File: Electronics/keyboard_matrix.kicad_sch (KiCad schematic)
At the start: 5 parts, among them SW1 SW_SPST, SW2 SW_SPST, U1 STM32C011F6Px

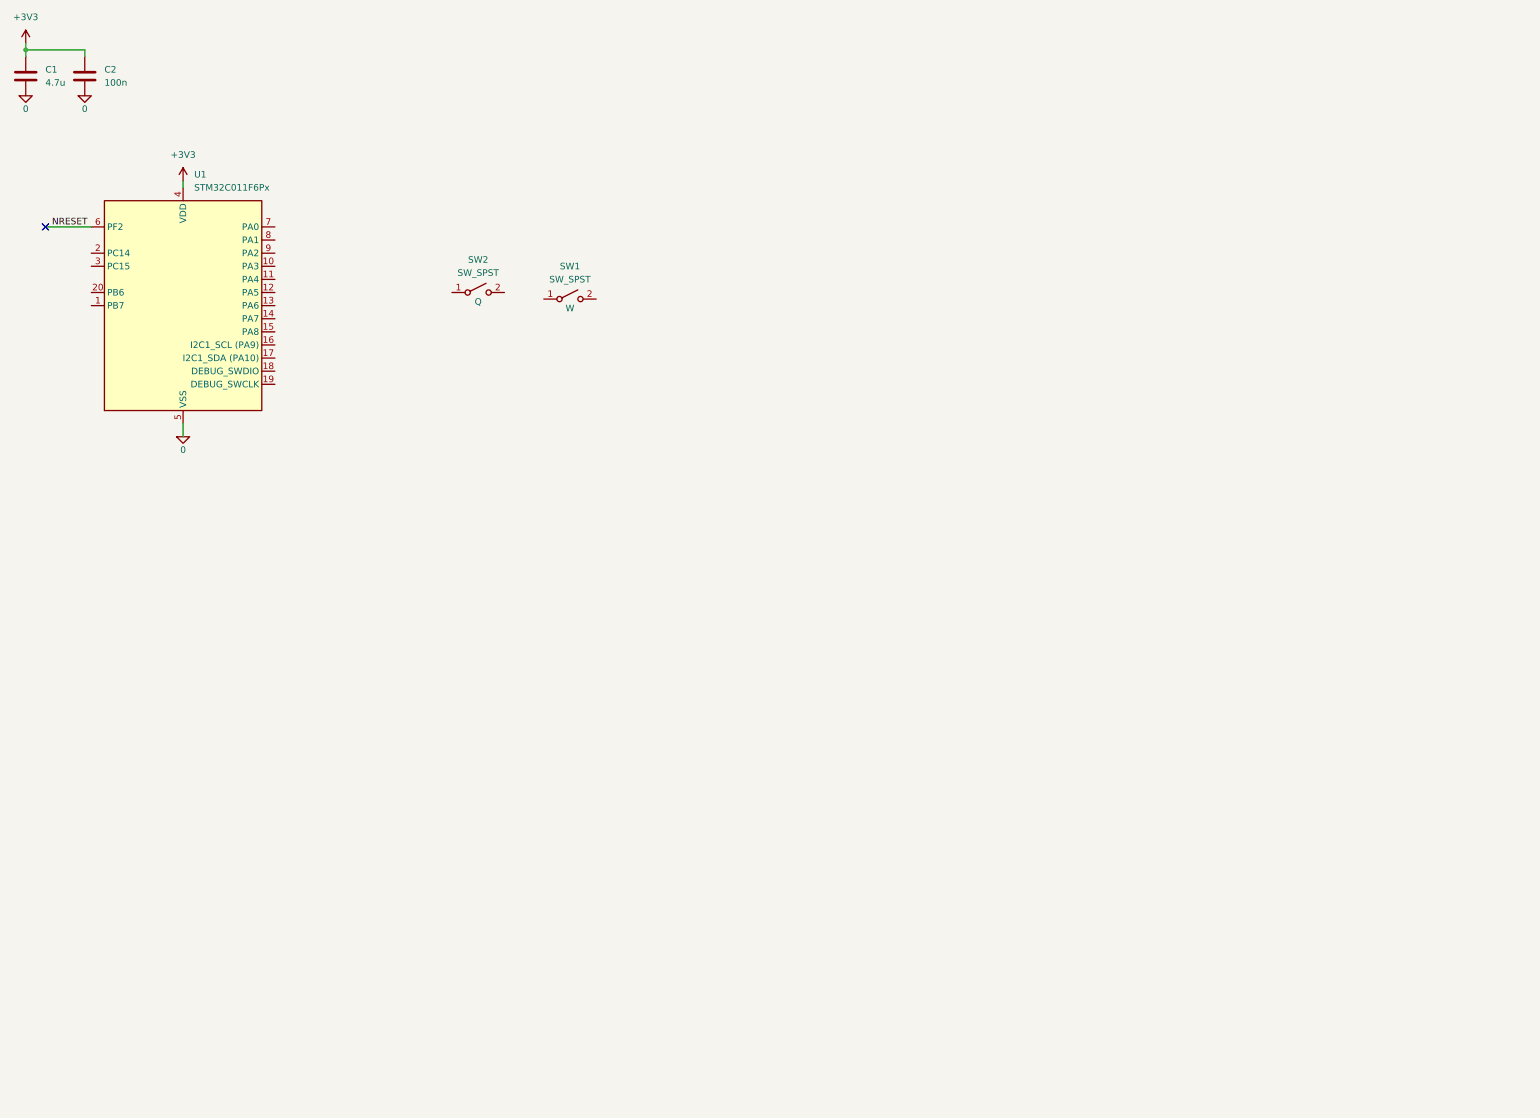
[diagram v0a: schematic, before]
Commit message: completed keyboard schematic. added design note for stm32c0
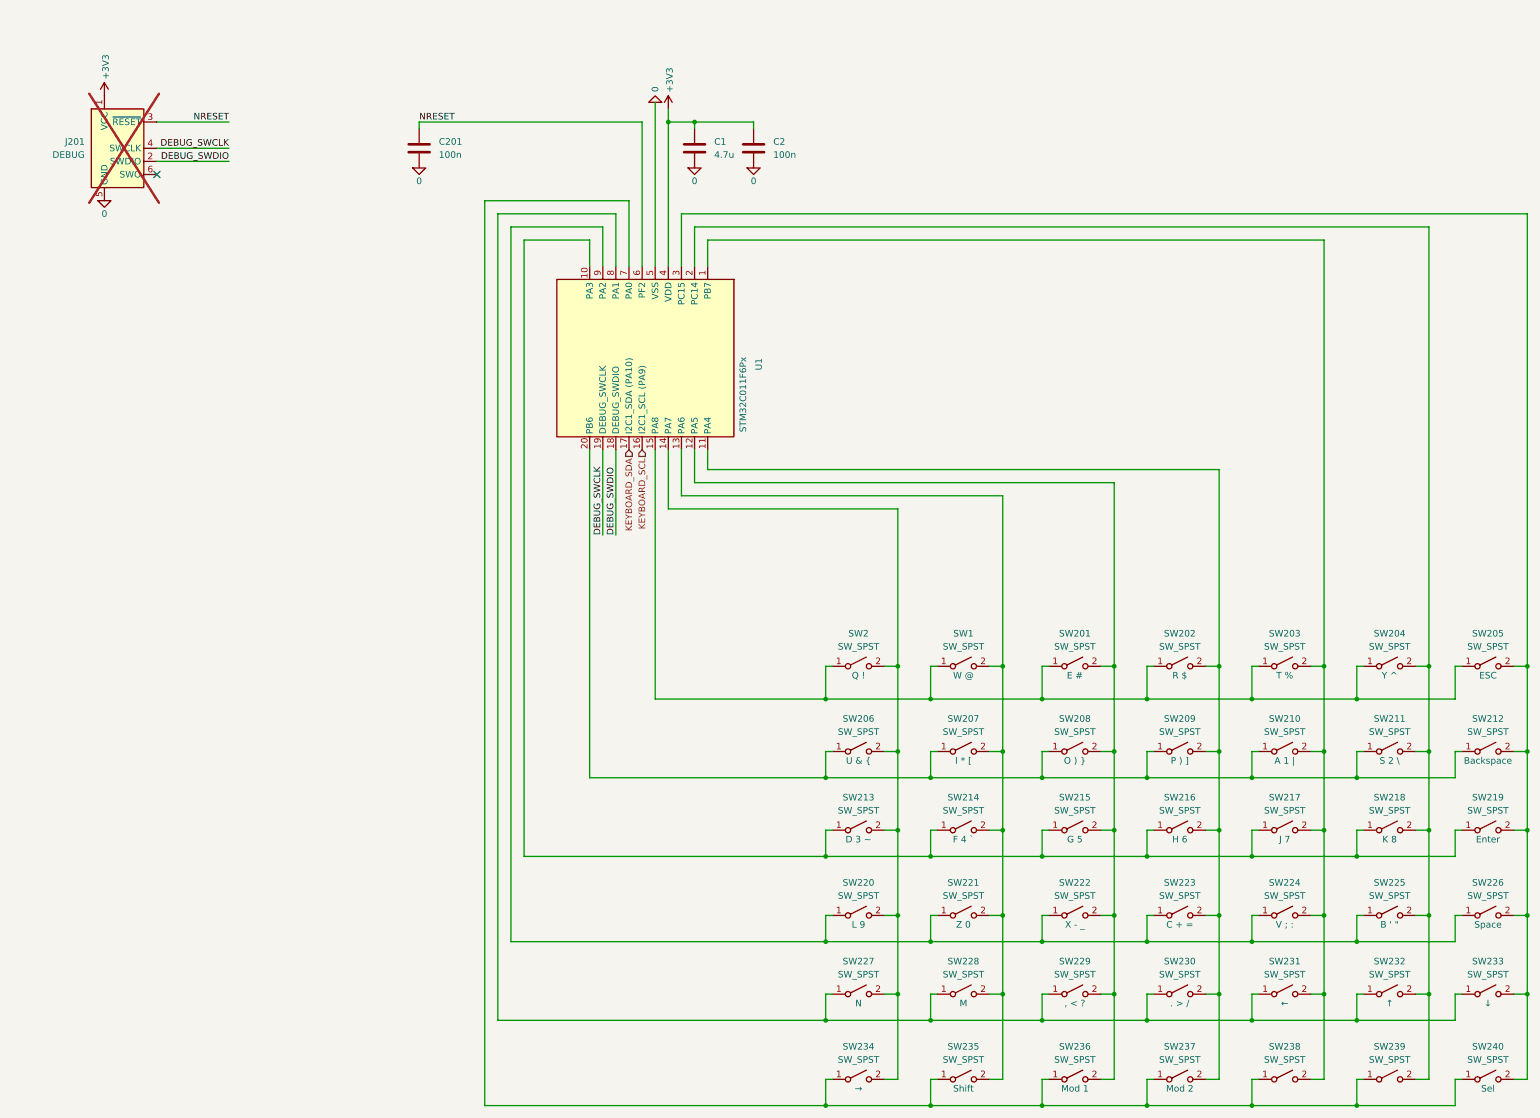
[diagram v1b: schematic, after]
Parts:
- added C201: 100n, Capacitor_SMD:C_0402_1005Metric_Pad0.74x0.62mm_HandSolder, symbol Device:C
- added J201: DEBUG, Connector:Tag-Connect_TC2030-IDC-FP_2x03_P1.27mm_Vertical, symbol Connector:Conn_ARM_SWD_TagConnect_TC2030
- added SW201, SW202, SW203, SW204, SW205, SW206, SW207, SW208, SW209, SW210, SW211, SW212, SW213, SW214, SW215, SW216, SW217, SW218, SW219, SW220, SW221, SW222, SW223, SW224, SW225, SW226, SW227, SW228, SW229, SW230, SW231, SW232, SW233, SW234, SW235, SW236, SW237, SW238, SW239, SW240: SW_SPST, Button_Switch_SMD:SW_Tactile_SPST_NO_Straight_CK_PTS636Sx25SMTRLFS, symbol Switch:SW_SPST
- SW1: Key Text W -> W @
- SW2: Key Text Q -> Q !
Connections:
- net +3V3: now also J201.1 (VCC)
- net 0: now also C201.2, J201.5 (GND)
- net NRESET: now also C201.1, J201.3 (~{RESET})
- net at SW2.1 (A): now also SW1.1 (A), U1.15 (PA8), SW201.1 (A), SW202.1 (A), SW203.1 (A), SW204.1 (A), SW205.1 (A)
- net at SW2.2 (B): now also U1.14 (PA7), SW206.2 (B), SW213.2 (B), SW220.2 (B), SW227.2 (B), SW234.2 (B)
- net at SW1.2 (B): now also U1.13 (PA6), SW207.2 (B), SW214.2 (B), SW221.2 (B), SW228.2 (B), SW235.2 (B)
- net at U1.1 (PB7): now also SW203.2 (B), SW210.2 (B), SW217.2 (B), SW224.2 (B), SW231.2 (B), SW238.2 (B)
- net at U1.10 (PA3): now also SW213.1 (A), SW214.1 (A), SW215.1 (A), SW216.1 (A), SW217.1 (A), SW218.1 (A), SW219.1 (A)
- net at U1.11 (PA4): now also SW202.2 (B), SW209.2 (B), SW216.2 (B), SW223.2 (B), SW230.2 (B), SW237.2 (B)
- net at U1.12 (PA5): now also SW201.2 (B), SW208.2 (B), SW215.2 (B), SW222.2 (B), SW229.2 (B), SW236.2 (B)
- net KEYBOARD_SCL: now reaches U1.16 (PA9/PA11)
- net KEYBOARD_SDA: now reaches U1.17 (PA10/PA12)
- net DEBUG_SWDIO: now reaches U1.18 (PA13)
- net DEBUG_SWDIO: now also J201.2 (SWDIO)
- net DEBUG_SWCLK: now reaches U1.19 (PA14)
- net DEBUG_SWCLK: now also J201.4 (SWCLK)
- net at U1.2 (PC14): now also SW204.2 (B), SW211.2 (B), SW218.2 (B), SW225.2 (B), SW232.2 (B), SW239.2 (B)
- net at U1.20 (PB6): now also SW206.1 (A), SW207.1 (A), SW208.1 (A), SW209.1 (A), SW210.1 (A), SW211.1 (A), SW212.1 (A)
- net at U1.3 (PC15): now also SW205.2 (B), SW212.2 (B), SW219.2 (B), SW226.2 (B), SW233.2 (B), SW240.2 (B)
- net at U1.7 (PA0): now also SW234.1 (A), SW235.1 (A), SW236.1 (A), SW237.1 (A), SW238.1 (A), SW239.1 (A), SW240.1 (A)
- net at U1.8 (PA1): now also SW227.1 (A), SW228.1 (A), SW229.1 (A), SW230.1 (A), SW231.1 (A), SW232.1 (A), SW233.1 (A)
- net at U1.9 (PA2): now also SW220.1 (A), SW221.1 (A), SW222.1 (A), SW223.1 (A), SW224.1 (A), SW225.1 (A), SW226.1 (A)
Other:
- company: (none) -> Bjorn Hropot
- title: (none) -> Keyboard
- moved on the sheet: C1, C2, SW1, SW2, U1

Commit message: arranged keys for keyboard. marked out lcd
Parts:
- SW40: renamed from SW238; Key Text (none) -> TAB
- renumbered C201 to C1, C1 to C2, C2 to C3, J201 to J1, SW2 to SW1, SW208 to SW10, SW209 to SW11, SW210 to SW12, SW211 to SW13, SW212 to SW14, SW213 to SW15, SW214 to SW16, SW215 to SW17, SW216 to SW18, SW217 to SW19, SW1 to SW2, SW218 to SW20, SW219 to SW21, SW220 to SW22, SW221 to SW23, SW222 to SW24, SW223 to SW25, SW224 to SW26, SW225 to SW27, SW226 to SW28, SW227 to SW29, SW201 to SW3, SW228 to SW30, SW229 to SW31, SW230 to SW32, SW231 to SW33, SW232 to SW34, SW233 to SW35, SW234 to SW36, SW235 to SW37, SW236 to SW38, SW237 to SW39, SW202 to SW4, SW239 to SW41, SW240 to SW42, SW203 to SW5, SW204 to SW6, SW205 to SW7, SW206 to SW8, SW207 to SW9
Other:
- company: Bjorn Hropot -> WebWow

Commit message: basic power supply layout some minor design notes. charge ic likely to change. possibly bridge out fuel gague
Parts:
- SW41: now not fitted
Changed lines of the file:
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@@
 		(in_bom yes)
 		(on_board yes)
-		(dnp no)
+		(dnp yes)
 		(property "Reference" "SW41"
 			(at 307.34 219.71 0)
